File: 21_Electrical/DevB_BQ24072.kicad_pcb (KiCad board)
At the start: 4 copper layers, 100 x 100 mm, 105 parts, among them J1 USB4135-GF-A_REVA, J3 SWD1, J8 Conn_01x07_Pin, SW1 BTN, SW2 BOOT0, T1 SWEB_8094, T2 SWEB_8094, T3 SWEB_8094, T4 SWEB_8094, U1 BQ24072RGT, U2 STM32F030F4Px

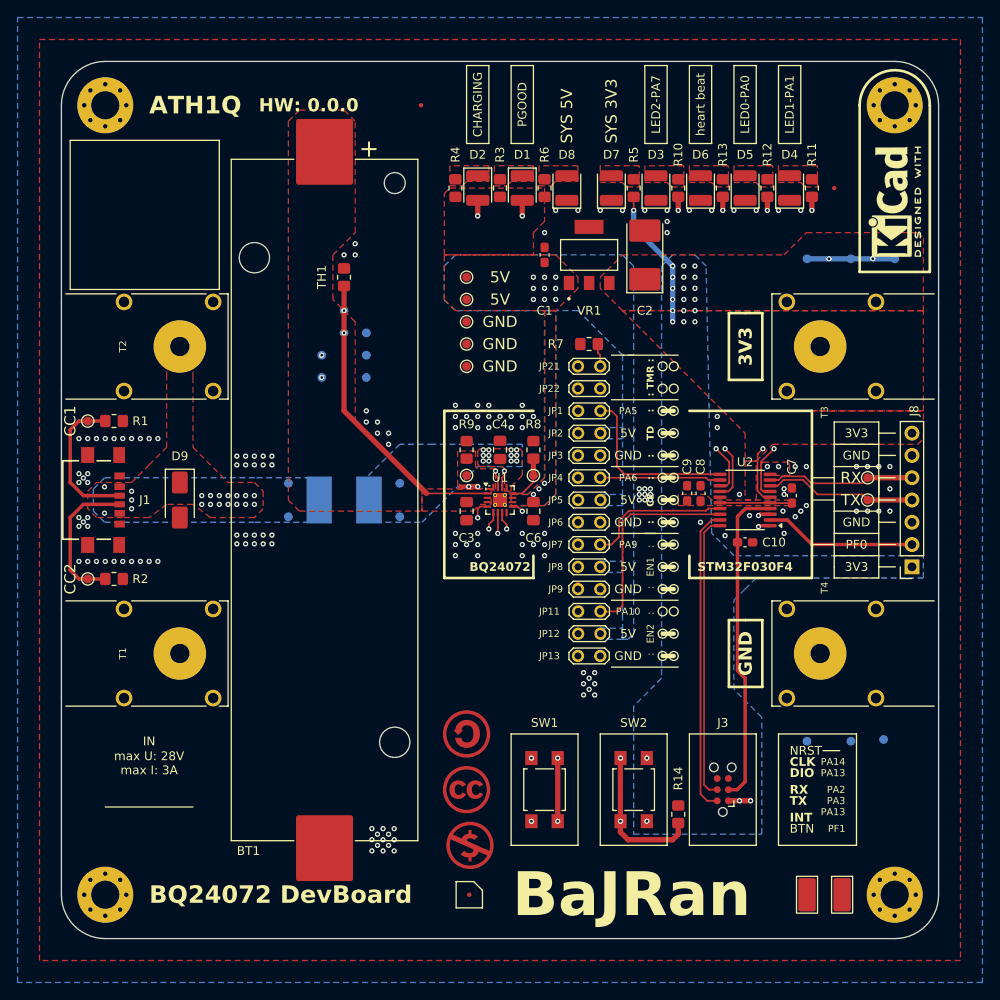
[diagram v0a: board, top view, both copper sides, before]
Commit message: PCB added SWD programateor connectors, README.MD update
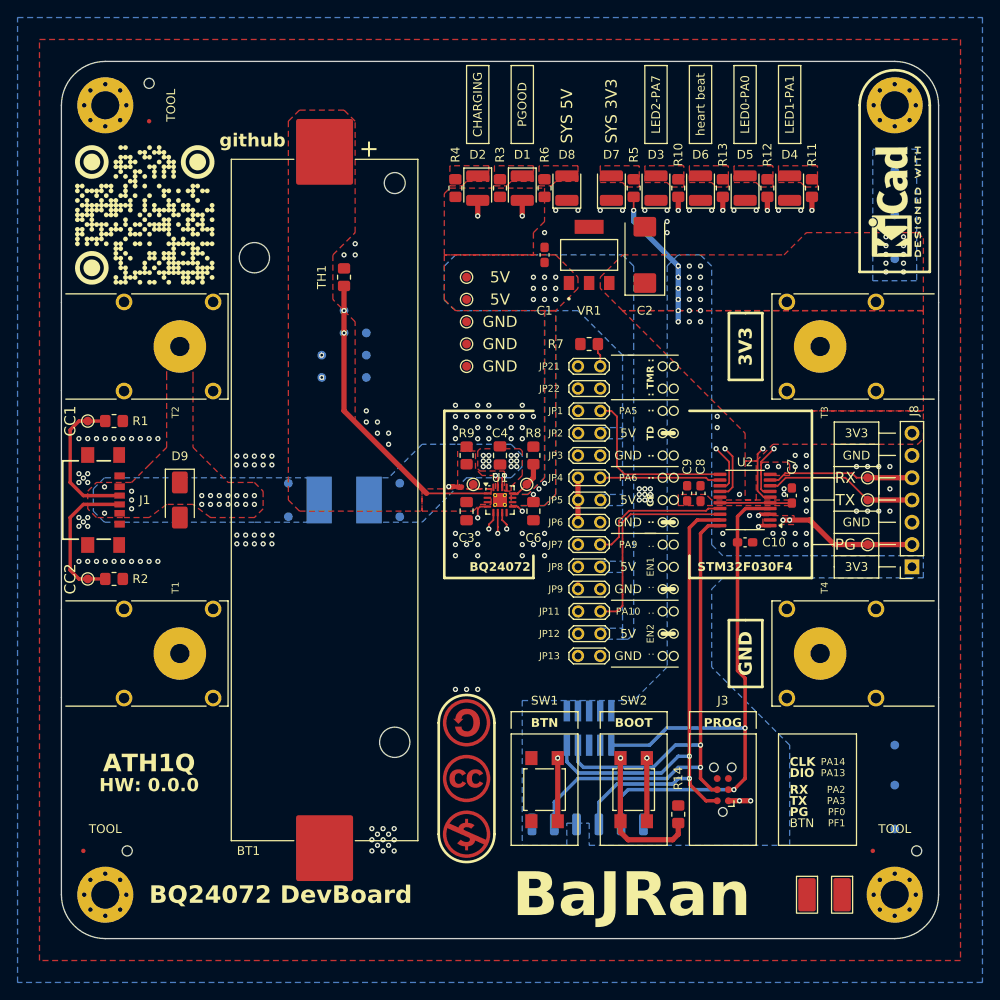
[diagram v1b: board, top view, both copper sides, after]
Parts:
- added G***: LOGO, __URL:URL_17mm, F.Cu at (61.2, 57.5)
- added G***: LOGO, __URL:URL_20mm, B.Cu at (71.8, 125.0)
- added H5: MountingHole_Pad, MountingHole:ToolingHole_1.152mm, F.Cu at (149.2, 130.0)
- added H6: MountingHole_Pad, MountingHole:ToolingHole_1.152mm, F.Cu at (59.2, 130.0)
- added H7: MountingHole_Pad, MountingHole:ToolingHole_1.152mm, F.Cu at (61.8, 42.5)
- added J2: Conn_ARM_JTAG_SWD_10, Connector_PinHeader_1.27mm:PinHeader_2x05_P1.27mm_Vertical_SMD, B.Cu at (111.9, 116.0)
- added J4: Conn_01x06_Pin, Connector_Harwin:Harwin_M20-89006xx_1x06_P2.54mm_Horizontal, B.Cu at (111.8, 132.5)
- added TP21: PG, TestPoint:TestPoint_Pad_D1.0mm, F.Cu at (143.7, 95.1)
- C2: footprint Capacitor_Tantalum_SMD:CP_EIA-7132-28_AVX-C -> Capacitor_Tantalum_SMD:CP_EIA-7343-31_Kemet-D_HandSolder
- C3, C6: value 4u7/16V -> 4u7/35V
- C4: value 4u7/50V -> 4u7/35V
- R10, R11, R12: value 400 -> 1k
- R13, R3, R4: value 10k -> 1k
- R7: value 10k -> XX
- R8: value 10k -> 1k15
- R9: value 10k -> 0k65
- moved FID3 99.4 mm to (144.2, 130.0)
- moved FID2 78.5 mm to (61.8, 46.8)
- moved FID1 44.3 mm to (54.2, 130.0)
- moved TP10 14.1 mm to (146.8, 52.5)
- moved TP12 10.3 mm to (146.8, 127.5), turned to -90 degrees
- moved TP26 10.0 mm to (146.8, 117.9), turned to 90 degrees
- moved TP25 7.07 mm to (146.8, 122.5), turned to 90 degrees
- moved TP9 7.07 mm to (146.8, 57.5)
- moved REF** 3.00 mm to (66.8, 45.0)
- moved REF** 1.33 mm to (97.9, 128.1)
- moved REF** 1.27 mm to (97.9, 115.4)
- moved REF** 1.27 mm to (97.9, 121.8)
- moved TP14 1.27 mm to (104.8, 88.2)
- moved TP15 1.27 mm to (98.7, 88.2)
- moved NT2 0.76 mm to (96.9, 88.5), turned to 180 degrees
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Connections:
- net /BQ_isense renamed /STM_isense
- J8 pad 2: /PF0 -> /LED_PG
- U2 pad 2: /PF0 -> /LED_PG
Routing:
- net /LED_PG: track 49.1 -> 101.9 mm, vias 2 -> 4
- net /SW_CLK: track 32.6 -> 70.3 mm, vias 0 -> 2
- net /SW_NRST: track 37.0 -> 69.2 mm, vias 0 -> 2
- net /SW_DIO: track 34.9 -> 66.9 mm, vias 0 -> 2
- net /PF0: track 17.3 -> 0.00 mm
- net /BTN_boot: track 71.7 -> 64.5 mm, vias 3 -> 2
- net /BTN: track 63.9 -> 56.8 mm, vias 3 -> 2
- net /PWR_SYS_3V3: track 36.9 -> 34.3 mm, vias 25 -> 32
- net /STM_isense: track 37.3 -> 39.1 mm, vias 4 -> 3
- net /LED_hG: track 49.7 -> 50.8 mm
- net /BQ_ilim: track 5.59 -> 4.65 mm
- net GND: vias 161 -> 165
- added copper zone on F.Cu, net /LED_PG
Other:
- board text added: "0"
- board text added: "BOOT"
- board text added: "GITHUB"
- board text added: "HW"
- board text added: "NC"
- board text added: "PG"
- board text added: "PROG"
- board text added: "SW"
- board text added: "TOOL"
- board text added: "X"
- board text added: "github"
- board text removed: "IN"
- board text removed: "INT"
- board text removed: "max U: 28V max I: 3A"
